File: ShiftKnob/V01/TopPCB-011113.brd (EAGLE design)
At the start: 33 x 33 mm, 6 parts

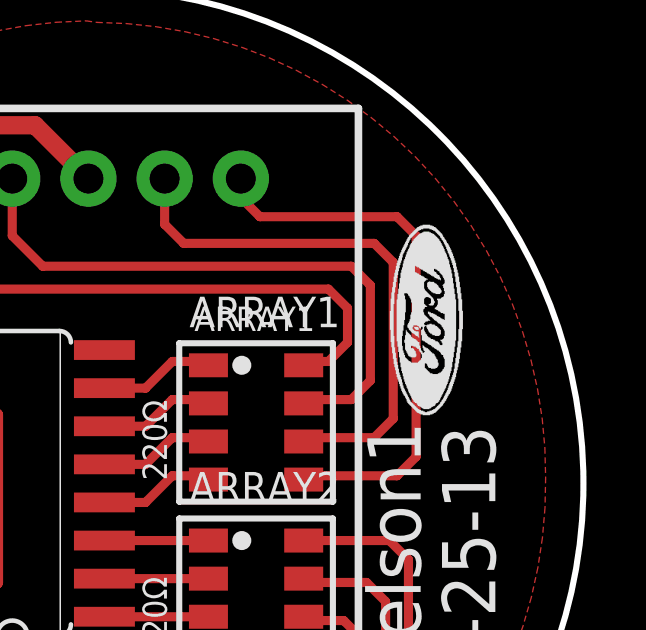
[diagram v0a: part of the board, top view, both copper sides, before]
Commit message: add open hardware logo
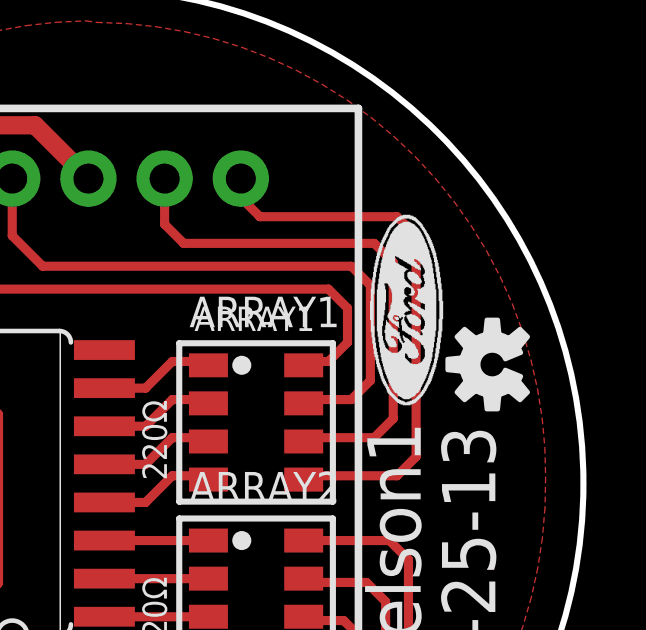
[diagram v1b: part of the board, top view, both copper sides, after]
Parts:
- added U$1, U$2: OSHW-LOGOS, SparkFun:OSHW-LOGO-S

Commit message: adjust silk screen for vector font.
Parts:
- moved U$2 5.60 mm to (25.7, 22.9)
- moved U$1 0.61 mm to (31.5, 22.3)
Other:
- board text added: "01-28-13"
- board text removed: "01-25-13"

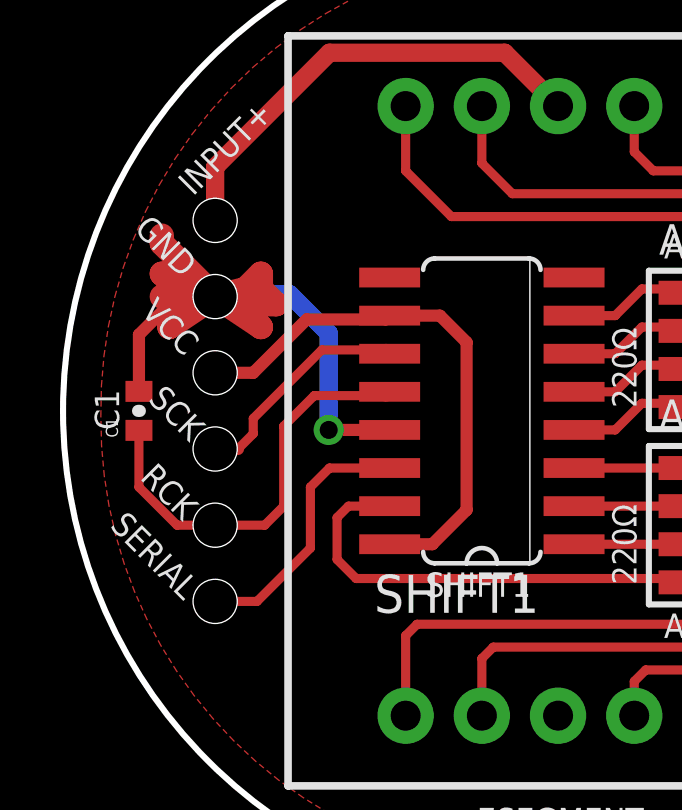
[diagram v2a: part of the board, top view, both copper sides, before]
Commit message: change 6 pin connector to match bottomPCB. run DRC and correct issues. move dimension callout to Document layer.
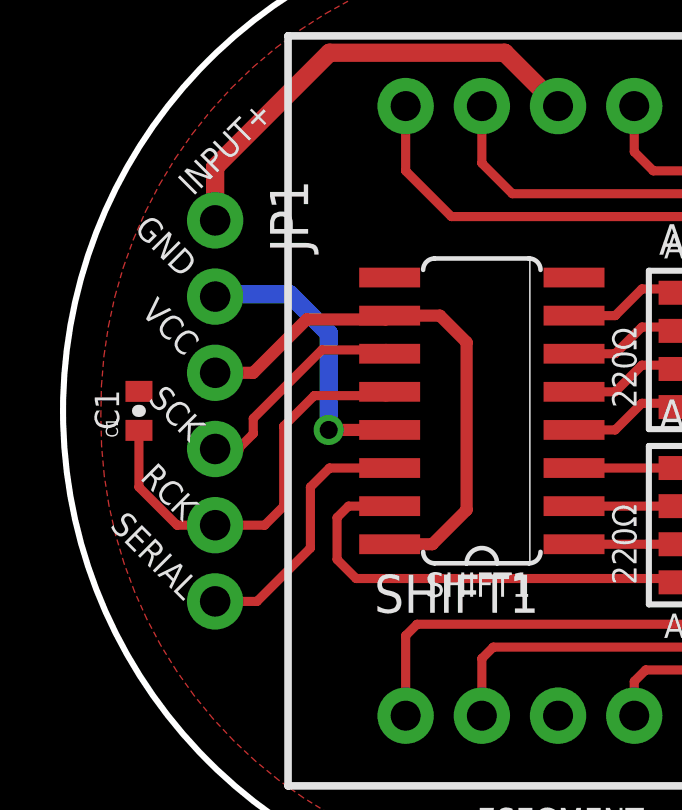
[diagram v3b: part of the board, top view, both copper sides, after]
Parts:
- JP1: device SparkFun-Connectors:1X06_HOLES_ONLY -> SparkFun-Connectors:1X06
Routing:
- net GND: track 36.0 -> 9.61 mm
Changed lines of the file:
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@@
 <layer number="42" name="bRestrict" color="1" fill="10" visible="yes" active="yes"/>
 <layer number="43" name="vRestrict" color="2" fill="10" visible="yes" active="yes"/>
-<layer number="44" name="Drills" color="7" fill="1" visible="no" active="yes"/>
+<layer number="44" name="Drills" color="7" fill="1" visible="yes" active="yes"/>
 <layer number="45" name="Holes" color="7" fill="1" visible="yes" active="yes"/>
 <layer number="46" name="Milling" color="3" fill="1" visible="no" active="yes"/>
@@
 <rectangle x1="30.2133" y1="23.9903" x2="31.6611" y2="24.0157" layer="22" rot="R90"/>
 <rectangle x1="30.6451" y1="23.9903" x2="31.2801" y2="24.0157" layer="22" rot="R90"/>
-<dimension x1="17.844515625" y1="34.279875" x2="17.715484375" y2="1.280125" x3="43.7642" y3="17.6784" layer="20" dtype="diameter"/>
+<dimension x1="17.844515625" y1="34.279875" x2="17.715484375" y2="1.280125" x3="43.7642" y3="17.6784" layer="48" dtype="diameter"/>
 <text x="15.0876" y="3.7338" size="0.8128" layer="21" font="vector">7SEGMENT</text>
 </plain>
@@
 </class>
 </classes>
-<designrules name="default">
-<description language="de">&lt;b&gt;EAGLE Design Rules&lt;/b&gt;
+<designrules name="SSC-EAGLE-2Lyr_v1.0.0.3">
+<description language="en">&lt;b&gt;EAGLE Design Rules for *2* Layer Designs (DS)&lt;/b&gt;
 &lt;p&gt;
-Die Standard-Design-Rules sind so gewählt, dass sie für
-die meisten Anwendungen passen. Sollte ihre Platine
-besondere Anforderungen haben, treffen Sie die erforderlichen
-Einstellungen hier und speichern die Design Rules unter
-einem neuen Namen ab.</description>
-<description language="en">&lt;b&gt;EAGLE Design Rules&lt;/b&gt;
+This Sunstone Circuits 2 Layer .DRU has been set to cover our minimum requirements for our double sided products. For questions, comments, suggestions, please contact Sunstone Customer Support: &lt;p&gt;&lt;b&gt;Email:&lt;/b&gt;  mailto:support@sunstone.com&lt;br&gt;&lt;b&gt;Phone:&lt;/b&gt; 800-228-8198.&lt;p&gt; v1.1Mod10/16/07~Layers-core reversal.Distance C/D.Restring%.Supply G%.&lt;p&gt; v1.2 Mod12/06/07~Distance C/D to 20mils.&lt;p&gt;v1.3Mod12/12/07~Supply/Annulus Value to 12.5mils&lt;p&gt;1/15/08 SSC-EAGLE-2Lyr_v1.0.0.3~For Release&lt;p&gt;10/3/08 Description Edit.&lt;p&gt;
 &lt;p&gt;
-The default Design Rules have been set to cover
-a wide range of applications. Your particular design
-may have different requirements, so please make the
-necessary adjustments and save your customized
-design rules under a new name.</description>
+&lt;i&gt;Attention: Upon running the design check and making modifications, please remember to save any changes before closing the application and sending in your board file to Sunstone Circuits for conversion.&lt;i&gt;</description>
 <param name="layerSetup" value="(1*16)"/>
-<param name="mtCopper" value="0.035mm 0.035mm 0.035mm 0.035mm 0.035mm 0.035mm 0.035mm 0.035mm 0.035mm 0.035mm 0.035mm 0.035mm 0.035mm 0.035mm 0.035mm 0.035mm"/>
-<param name="mtIsolate" value="1.5mm 0.15mm 0.2mm 0.15mm 0.2mm 0.15mm 0.2mm 0.15mm 0.2mm 0.15mm 0.2mm 0.15mm 0.2mm 0.15mm 0.2mm"/>
-<param name="mdWireWire" value="8mil"/>
-<param name="mdWirePad" value="8mil"/>
-<param name="mdWireVia" value="8mil"/>
-<param name="mdPadPad" value="8mil"/>
-<param name="mdPadVia" value="8mil"/>
-<param name="mdViaVia" value="8mil"/>
-<param name="mdSmdPad" value="8mil"/>
-<param name="mdSmdVia" value="8mil"/>
-<param name="mdSmdSmd" value="8mil"/>
+<param name="mtCopper" value="0.0178mm 0.0356mm 0.0356mm 0.0356mm 0.0356mm 0.0356mm 0.0356mm 0.0356mm 0.0356mm 0.0356mm 0.0356mm 0.0356mm 0.0356mm 0.0356mm 0.0356mm 0.0178mm"/>
+<param name="mtIsolate" value="59mil 0.1499mm 0.2007mm 0.1499mm 0.2007mm 0.1499mm 0.2007mm 0.1499mm 0.2007mm 0.1499mm 0.2007mm 0.1499mm 0.2007mm 0.1499mm 0.2007mm"/>
+<param name="mdWireWire" value="6mil"/>
+<param name="mdWirePad" value="6mil"/>
+<param name="mdWireVia" value="6mil"/>
+<param name="mdPadPad" value="6mil"/>
+<param name="mdPadVia" value="6mil"/>
+<param name="mdViaVia" value="6mil"/>
+<param name="mdSmdPad" value="6mil"/>
+<param name="mdSmdVia" value="6mil"/>
+<param name="mdSmdSmd" value="6mil"/>
 <param name="mdViaViaSameLayer" value="8mil"/>
 <param name="mnLayersViaInSmd" value="2"/>
-<param name="mdCopperDimension" value="40mil"/>
-<param name="mdDrill" value="8mil"/>
+<param name="mdCopperDimension" value="20mil"/>
+<param name="mdDrill" value="16mil"/>
 <param name="mdSmdStop" value="0mil"/>
-<param name="msWidth" value="10mil"/>
-<param name="msDrill" value="24mil"/>
-<param name="msMicroVia" value="9.99mm"/>
+<param name="msWidth" value="6mil"/>
+<param name="msDrill" value="14mil"/>
+<param name="msMicroVia" value="9.9898mm"/>
 <param name="msBlindViaRatio" value="0.5"/>
 <param name="rvPadTop" value="0.25"/>
@@
 <param name="rvMicroViaOuter" value="0.25"/>
 <param name="rvMicroViaInner" value="0.25"/>
-<param name="rlMinPadTop" value="10mil"/>
-<param name="rlMaxPadTop" value="20mil"/>
-<param name="rlMinPadInner" value="10mil"/>
-<param name="rlMaxPadInner" value="20mil"/>
-<param name="rlMinPadBottom" value="10mil"/>
-<param name="rlMaxPadBottom" value="20mil"/>
+<param name="rlMinPadTop" value="8mil"/>
+<param name="rlMaxPadTop" value="999mil"/>
+<param name="rlMinPadInner" value="0mil"/>
+<param name="rlMaxPadInner" value="0mil"/>
+<param name="rlMinPadBottom" value="8mil"/>
+<param name="rlMaxPadBottom" value="999mil"/>
 <param name="rlMinViaOuter" value="8mil"/>
-<param name="rlMaxViaOuter" value="20mil"/>
-<param name="rlMinViaInner" value="8mil"/>
-<param name="rlMaxViaInner" value="20mil"/>
-<param name="rlMinMicroViaOuter" value="4mil"/>
-<param name="rlMaxMicroViaOuter" value="20mil"/>
-<param name="rlMinMicroViaInner" value="4mil"/>
-<param name="rlMaxMicroViaInner" value="20mil"/>
+<param name="rlMaxViaOuter" value="999mil"/>
+<param name="rlMinViaInner" value="0mil"/>
+<param name="rlMaxViaInner" value="0mil"/>
+<param name="rlMinMicroViaOuter" value="8mil"/>
+<param name="rlMaxMicroViaOuter" value="999mil"/>
+<param name="rlMinMicroViaInner" value="0mil"/>
+<param name="rlMaxMicroViaInner" value="0mil"/>
 <param name="psTop" value="-1"/>
 <param name="psBottom" value="-1"/>
@@
 <param name="mvStopFrame" value="1"/>
 <param name="mvCreamFrame" value="0"/>
-<param name="mlMinStopFrame" value="4mil"/>
-<param name="mlMaxStopFrame" value="4mil"/>
+<param name="mlMinStopFrame" value="3mil"/>
+<param name="mlMaxStopFrame" value="3mil"/>
 <param name="mlMinCreamFrame" value="0mil"/>
 <param name="mlMaxCreamFrame" value="0mil"/>
@@
 <param name="checkRestrict" value="1"/>
 <param name="useDiameter" value="13"/>
-<param name="maxErrors" value="50"/>
+<param name="maxErrors" value="500"/>
 </designrules>
 <autorouter>
@@
 <element name="7SEGMENT" library="SparkFun-Displays" package="7-SEGMENT-1&quot;PTH" value="7-SEGMENT-DISPLAY-1&quot;-RED" x="17.78" y="17.78"/>
 <element name="SHIFT1" library="74xx-eu" package="SO16" value="74HC595D" x="15.24" y="17.78" rot="R90"/>
-<element name="JP1" library="SparkFun-Connectors" package="1X06_HOLES_ONLY" value="6 PIN 90degree Header" x="6.35" y="24.13" rot="R270"/>
+<element name="JP1" library="SparkFun-Connectors" package="1X06" value="6 PIN 90degree Header" x="6.35" y="24.13" rot="R270"/>
 <element name="C1" library="SparkFun-Capacitors" package="0402-CAP" value="0.1uF" x="3.81" y="17.78" rot="R90"/>
 <element name="ARRAY1" library="resistor-array" package="744-8" value="220" x="23.368" y="19.812" rot="R270"/>
@@
 <contactref element="C1" pad="2"/>
 <contactref element="JP1" pad="2"/>
-<wire x1="6.35" y1="21.59" x2="5.08" y2="21.59" width="0.4064" layer="1"/>
-<wire x1="5.08" y1="21.59" x2="3.81" y2="20.32" width="0.4064" layer="1"/>
-<wire x1="3.81" y1="20.32" x2="3.81" y2="18.43" width="0.4064" layer="1"/>
-<wire x1="4.572" y1="21.59" x2="6.35" y2="21.59" width="0.8128" layer="1"/>
-<wire x1="6.35" y1="21.59" x2="4.572" y2="22.352" width="0.8128" layer="1"/>
-<wire x1="4.572" y1="22.352" x2="5.588" y2="21.336" width="0.8128" layer="1"/>
-<wire x1="5.588" y1="21.336" x2="8.382" y2="21.336" width="0.8128" layer="1"/>
-<wire x1="8.382" y1="21.336" x2="7.874" y2="21.844" width="0.8128" layer="1"/>
-<wire x1="7.874" y1="21.844" x2="7.874" y2="22.352" width="0.8128" layer="1"/>
-<wire x1="7.874" y1="22.352" x2="7.366" y2="21.844" width="0.8128" layer="1"/>
-<wire x1="7.366" y1="21.844" x2="6.35" y2="21.59" width="0.8128" layer="1"/>
-<wire x1="6.35" y1="21.59" x2="7.874" y2="20.574" width="0.8128" layer="1"/>
-<wire x1="7.874" y1="20.574" x2="6.858" y2="21.59" width="0.8128" layer="1"/>
-<wire x1="6.858" y1="21.59" x2="6.35" y2="21.59" width="0.8128" layer="1"/>
-<wire x1="6.35" y1="21.59" x2="4.826" y2="20.574" width="0.8128" layer="1"/>
-<wire x1="4.826" y1="20.574" x2="4.826" y2="20.828" width="0.8128" layer="1"/>
-<wire x1="4.826" y1="20.828" x2="5.588" y2="21.59" width="0.8128" layer="1"/>
-<wire x1="5.588" y1="21.59" x2="6.35" y2="21.59" width="0.8128" layer="1"/>
-<wire x1="6.35" y1="21.59" x2="4.572" y2="23.368" width="0.8128" layer="1"/>
-<wire x1="4.572" y1="23.368" x2="4.572" y2="23.622" width="0.8128" layer="1"/>
-<polygon width="0.4064" layer="1" isolate="0.4064">
+<polygon width="0.6096" layer="1" isolate="0.4064">
 <vertex x="2.54" y="17.6022" curve="-90"/>
 <vertex x="17.7038" y="33.1978"/>
